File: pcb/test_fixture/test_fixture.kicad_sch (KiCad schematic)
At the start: 80 parts, among them J1 UART, J3 Conn_ARM_JTAG_SWD_10, J5 GND, J6 GND, P3.3V1 , U1 SC0915, U2 MIC29302WU, U3 INA186A5IDCKR, U4 INA186A5IDCKR

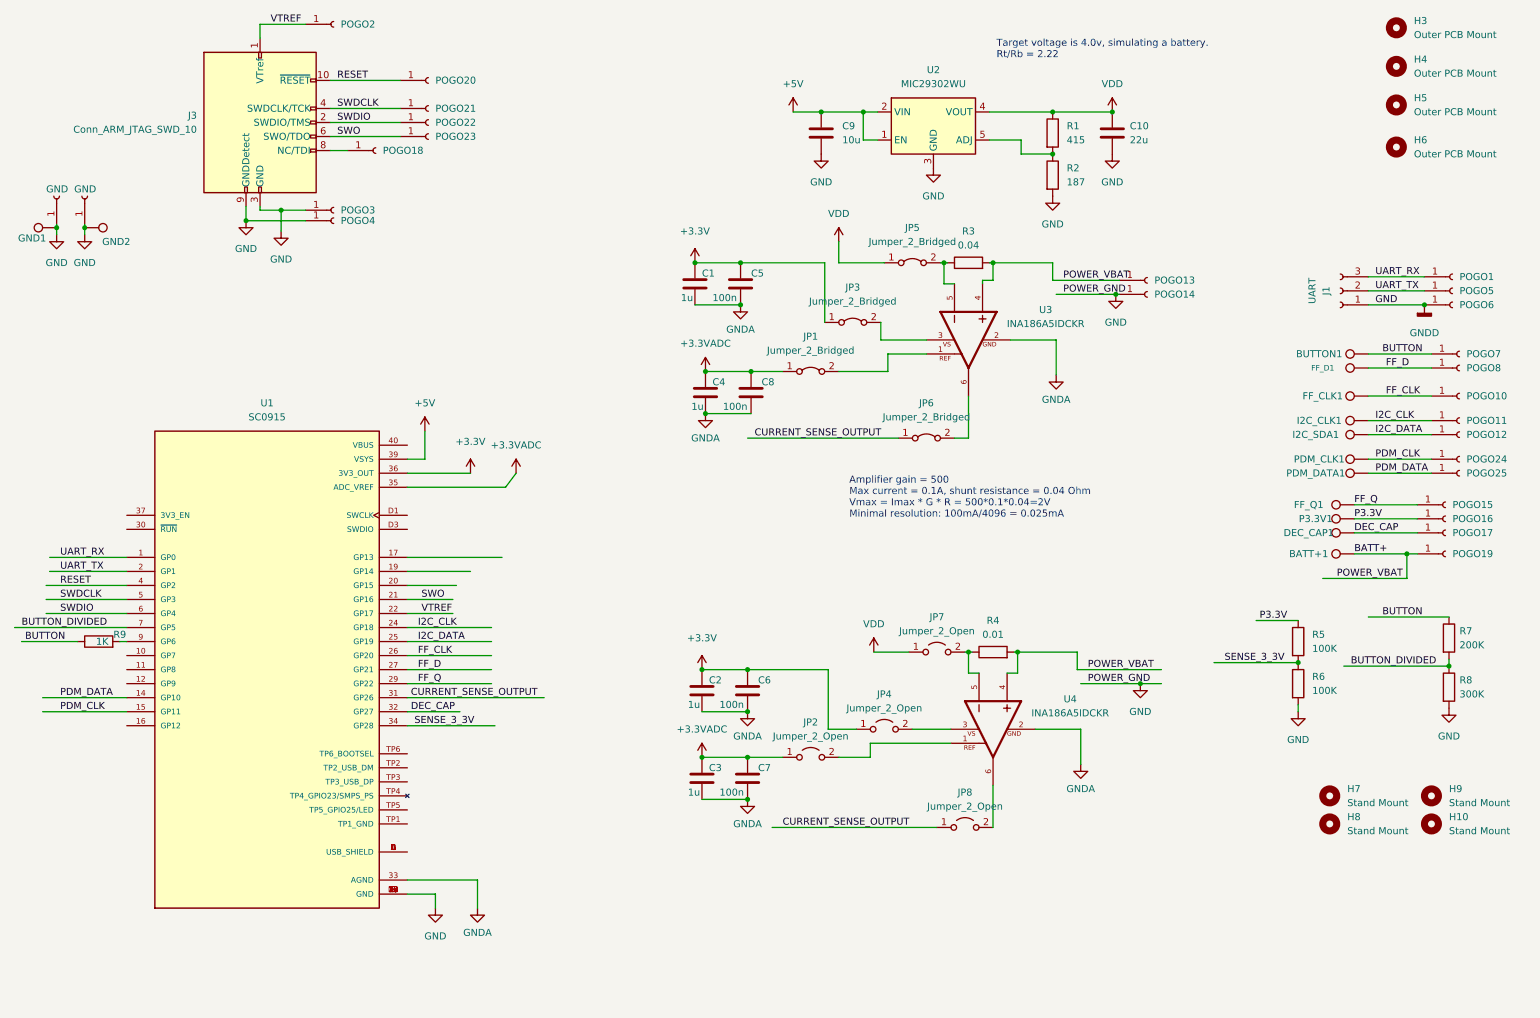
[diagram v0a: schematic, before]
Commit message: fixed another issue (added current limiting resistor, added testpoint for button control)
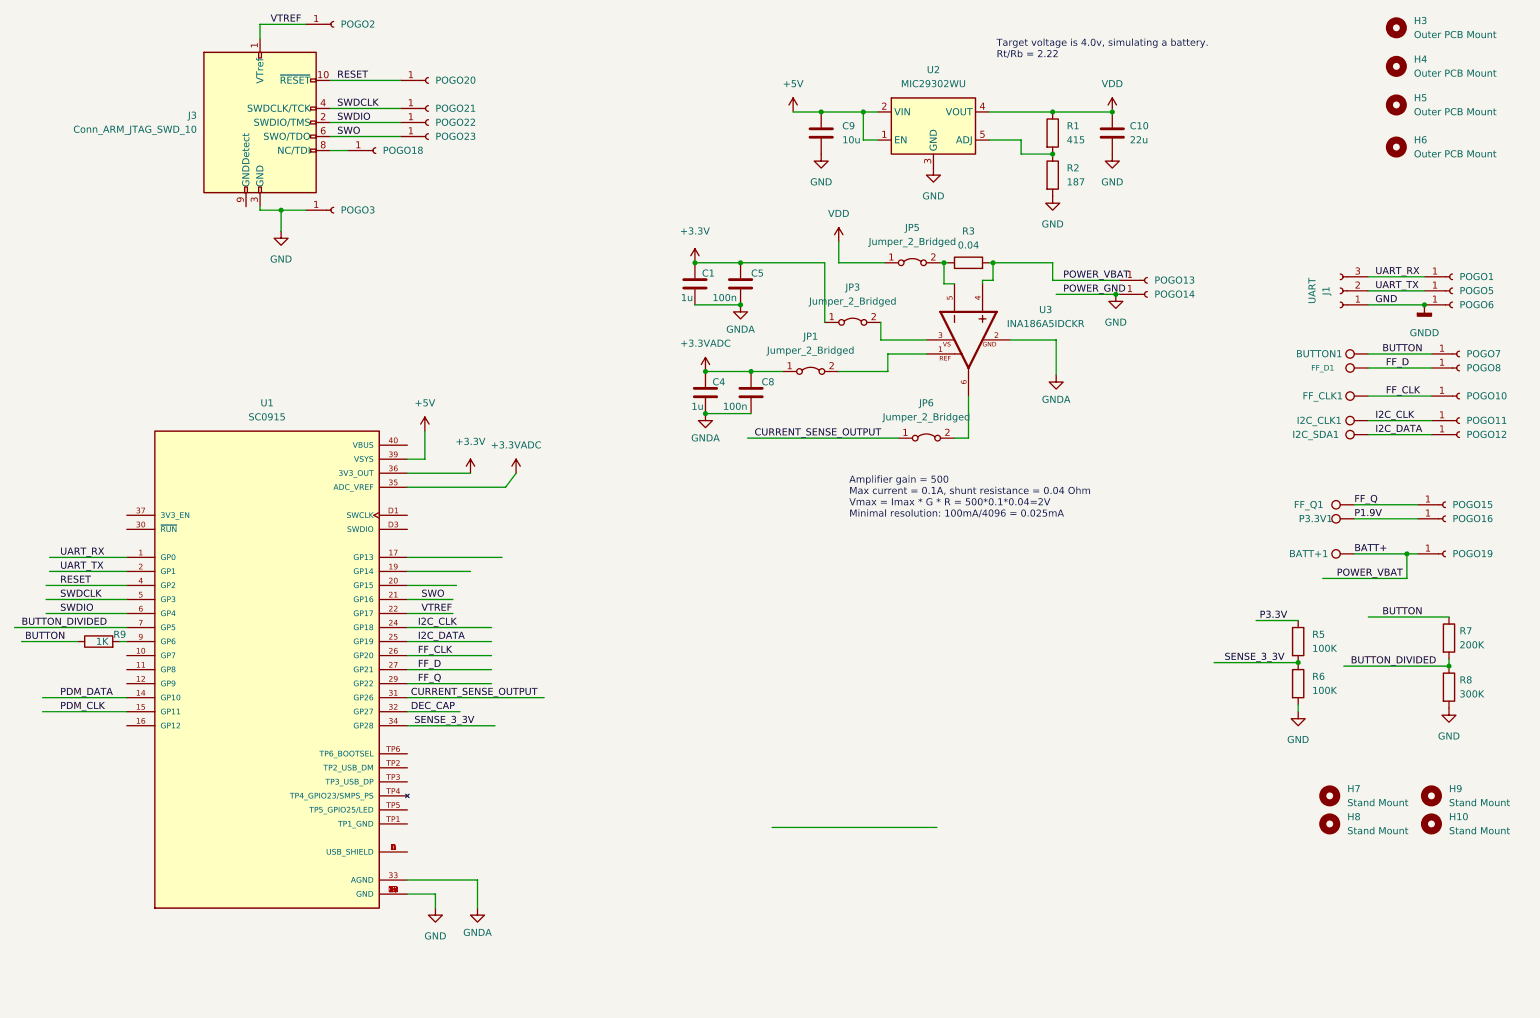
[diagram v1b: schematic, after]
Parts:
- removed C2, C3: 1u, Resistor_SMD:R_1206_3216Metric, symbol Device:C
- removed C6, C7: 100n, Resistor_SMD:R_1206_3216Metric, symbol Device:C
- removed DEC_CAP1, GND1, GND2, PDM_CLK1, PDM_DATA1: (no value), TestPoint:TestPoint_Pad_D1.5mm, symbol Connector:TestPoint
- removed J5, J6: GND, fixture:POGO, symbol Connector:Conn_01x01_Female
- removed JP2, JP4, JP7, JP8: Jumper_2_Open, Jumper:SolderJumper-2_P1.3mm_Open_RoundedPad1.0x1.5mm, symbol Jumper:Jumper_2_Open
- removed POGO17, POGO24, POGO25, POGO4: pogo, fixture:POGO, symbol Connector:Conn_01x01_Female
- removed R4: 0.01, Resistor_SMD:R_Shunt_Vishay_WSR2_WSR3_KelvinConnection, symbol Device:R
- removed U4: INA186A5IDCKR, SOT65P210X110-6N, symbol fixture:INA186A1IDCKR
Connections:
- net GND: no longer J3.9 (GNDDetect)
- net P3.3V: no longer P3.3V1.1, POGO16.1 (Pin_1)
- new net P1.9V: P3.3V1.1, POGO16.1 (Pin_1)

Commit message: fixing the state of harness for 1.4.52840
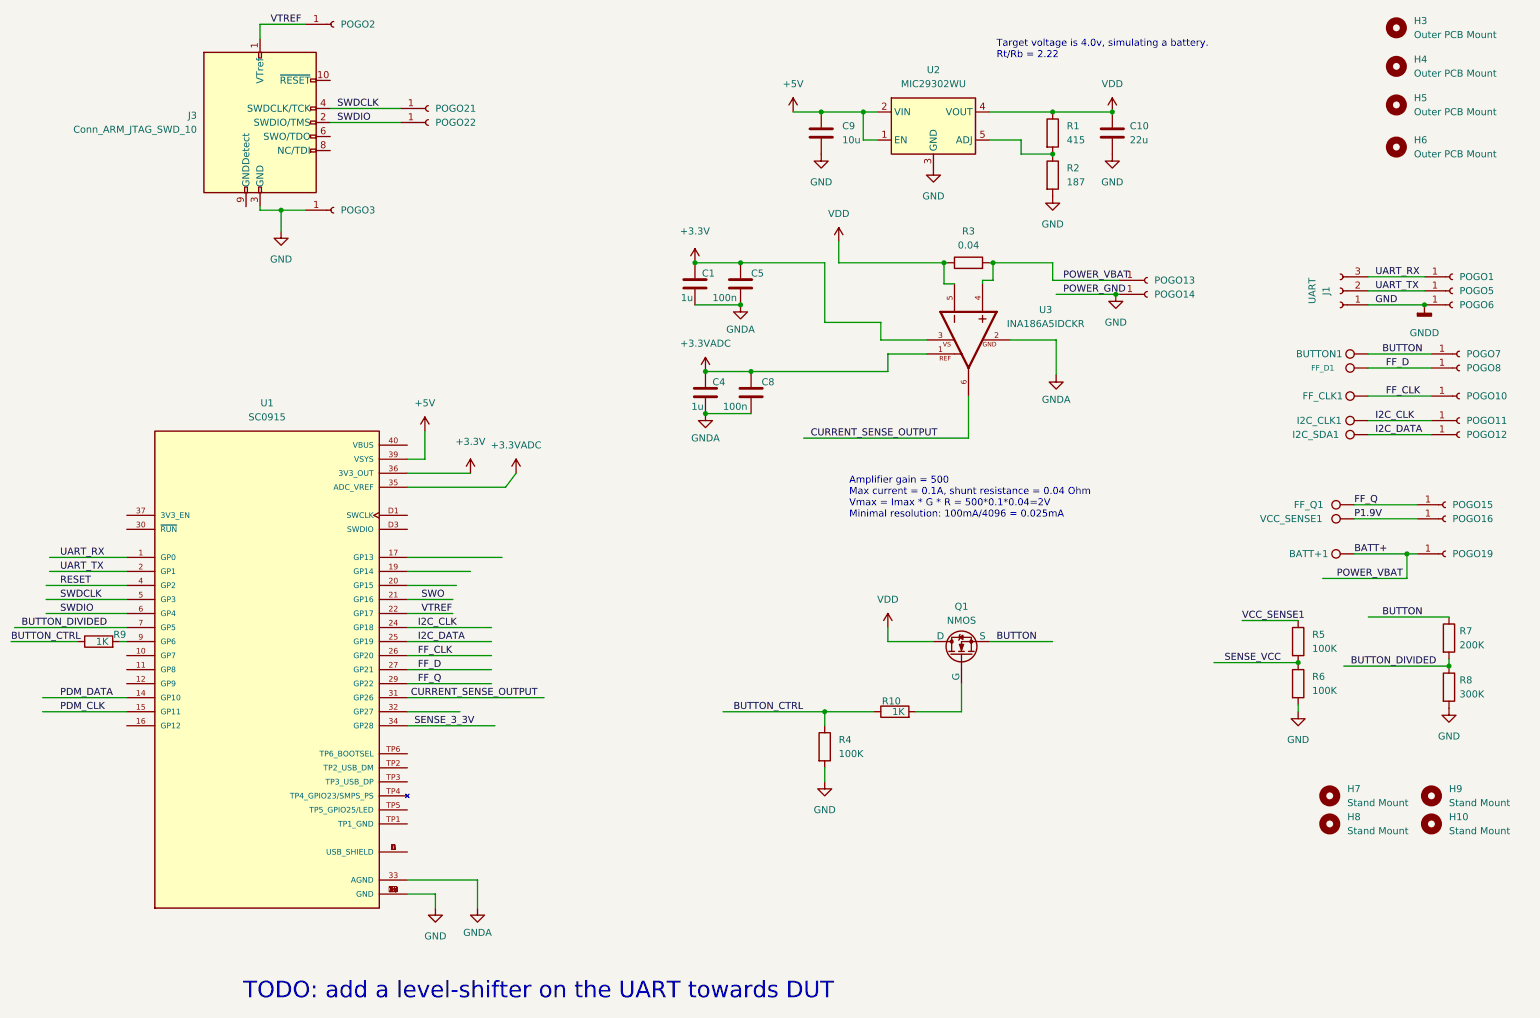
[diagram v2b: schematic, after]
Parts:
- removed JP1, JP3, JP5, JP6: Jumper_2_Bridged, Jumper:SolderJumper-2_P1.3mm_Bridged2Bar_Pad1.0x1.5mm, symbol Jumper:Jumper_2_Bridged
- removed POGO18, POGO20, POGO23: pogo, fixture:POGO, symbol Connector:Conn_01x01_Female
- added Q1: NMOS, Package_TO_SOT_SMD:SOT-23, symbol Simulation_SPICE:NMOS
- added R10: 1K, Resistor_SMD:R_0603_1608Metric, symbol Device:R
- added R4: 100K, Resistor_SMD:R_0603_1608Metric, symbol Device:R
- renumbered P3.3V1 to VCC_SENSE1
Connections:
- net +3.3V: now also U3.3
- net +3.3VADC: now also U3.1
- net BUTTON: now also Q1.3 (S); no longer R9.1
- net CURRENT_SENSE_OUTPUT: now also U3.6
- net GND: now also R4.2
- net RESET: no longer J3.10 (~{RESET})
- net SENSE_3_3V: no longer R5.2, R6.1
- net SWO: no longer J3.6 (SWO/TDO)
- net VDD: now also R3.1, U3.5, Q1.1 (D)
- net DEC_CAP: no longer names the net of U1.32 (GP27)
- net P3.3V renamed VCC_SENSE1
- new net: Q1.2 (G), R10.2
- new net BUTTON_CTRL: R10.1, R4.1, R9.1
- new net SENSE_VCC: R5.2, R6.1
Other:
- note added: "TODO: add a level-shifter on the UART towards DUT"
